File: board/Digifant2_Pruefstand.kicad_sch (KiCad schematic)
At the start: 44 parts, among them J0 VW ECU HARNESS, J1 12V BENCH IN, J2 IDLE VALVE N71, J3 OLED / UI I2C, Q1 2N7002, Q2 P-MOS -30V >=5A, Q3 2N7002, SW1 PUSH, SW2 PUSH, SW3 PUSH, U1 INA226 (0x40), U2 MCP4728 (0x60), U3 INA226 (0x41), U4 AD9833, U5 Raspberry Pi Pico, Y1 25MHz

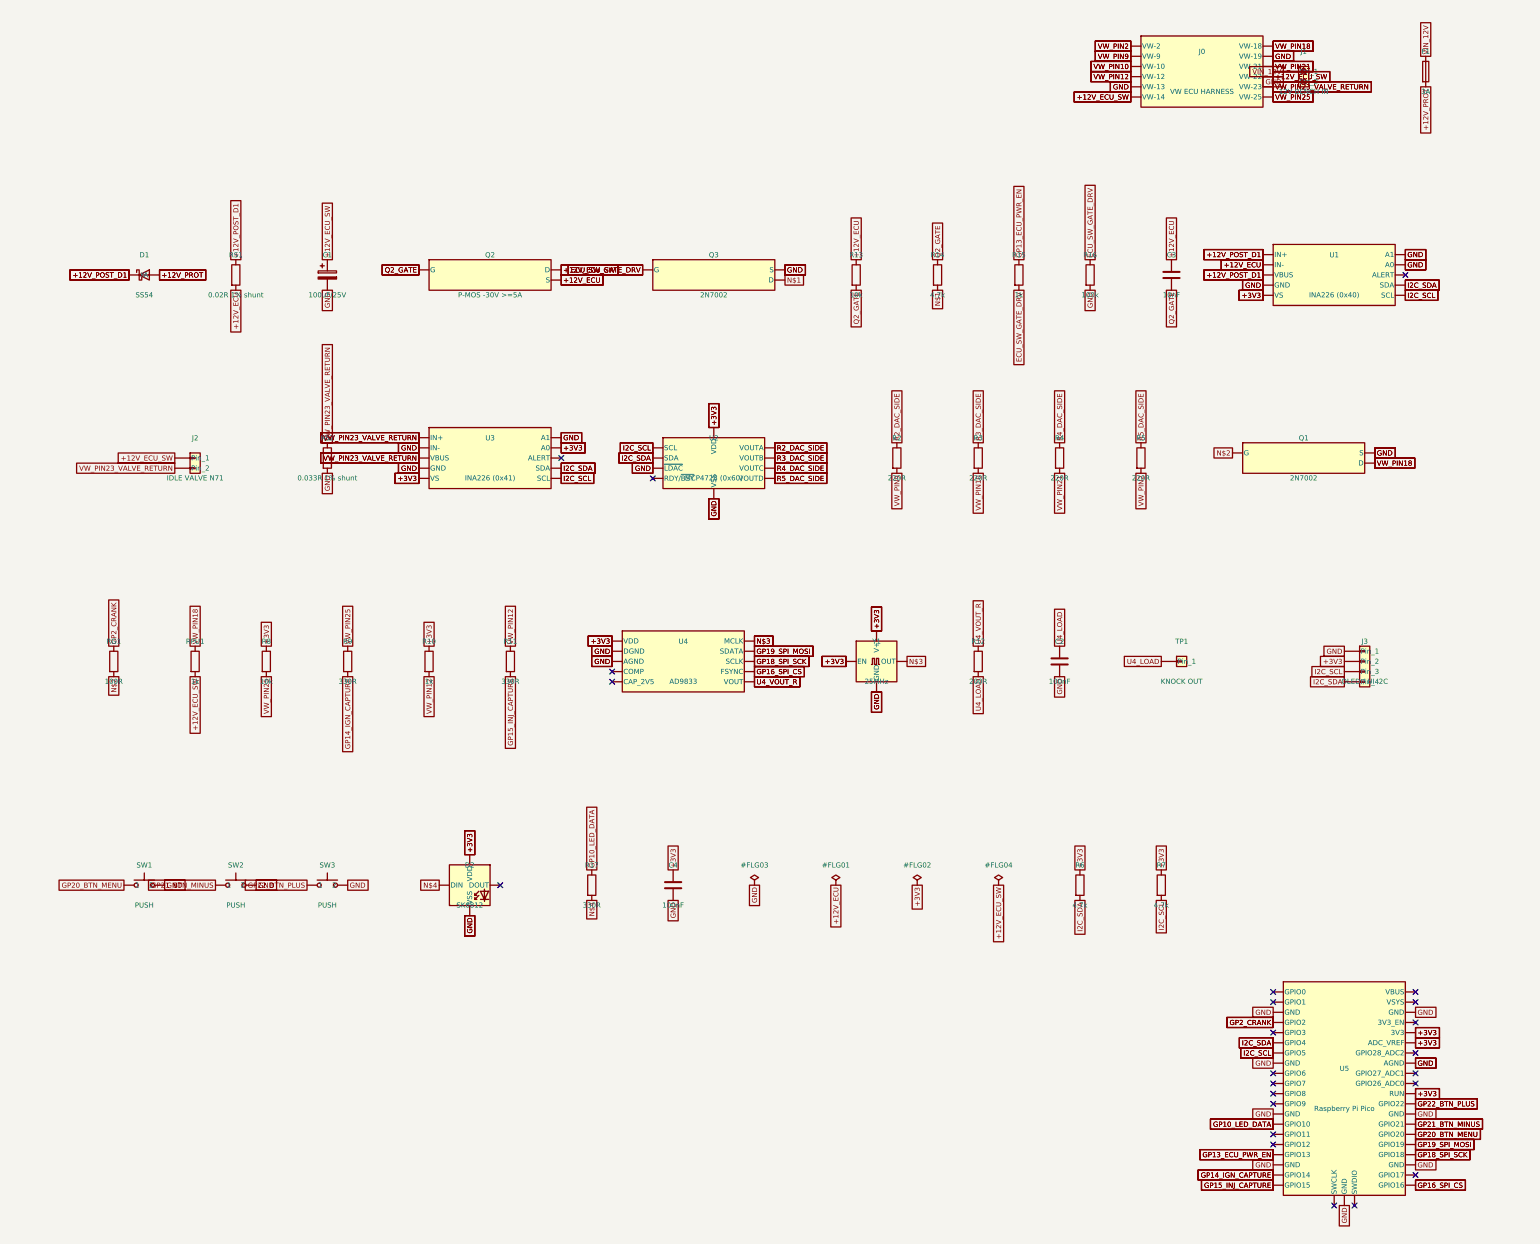
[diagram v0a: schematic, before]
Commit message: Verify VW pinout; add throttle switches, AFM ref sense, bus-voltage read
- verified the harness against the cabby-info.com Digifant II 25-pin reference;
  DESIGN.md now marks each pin confirmed / flagged (VW-8-vs-18 crank, VW-6/11
  idle-vs-WOT unresolved)
- J0 -> 15-pos terminal block; break out VW-6/11 (throttle switches) and VW-17
- throttle_switches(): Q4/Q5 open-drain emulate the idle + WOT micro-switches
  on GP6/GP7, fail-safe open
- afm_ref_sense(): R20/R21 divider + C5 feed VW-17 into GP26/ADC0 so the LMM
  sim can be scaled ratiometrically
- U1 VBUS moved to the shunt load side -> reads the ECU supply voltage;
  U3 VBUS on the valve supply rail -> reads valve feed voltage
- mounting holes flagged board-only (no more extra_footprint DRC)

Co-Authored-By: Claude Sonnet 5 <noreply@anthropic.com>
Claude-Session: https://claude.ai/code/session_01XcEuUwwCT37oProAm8HYeY
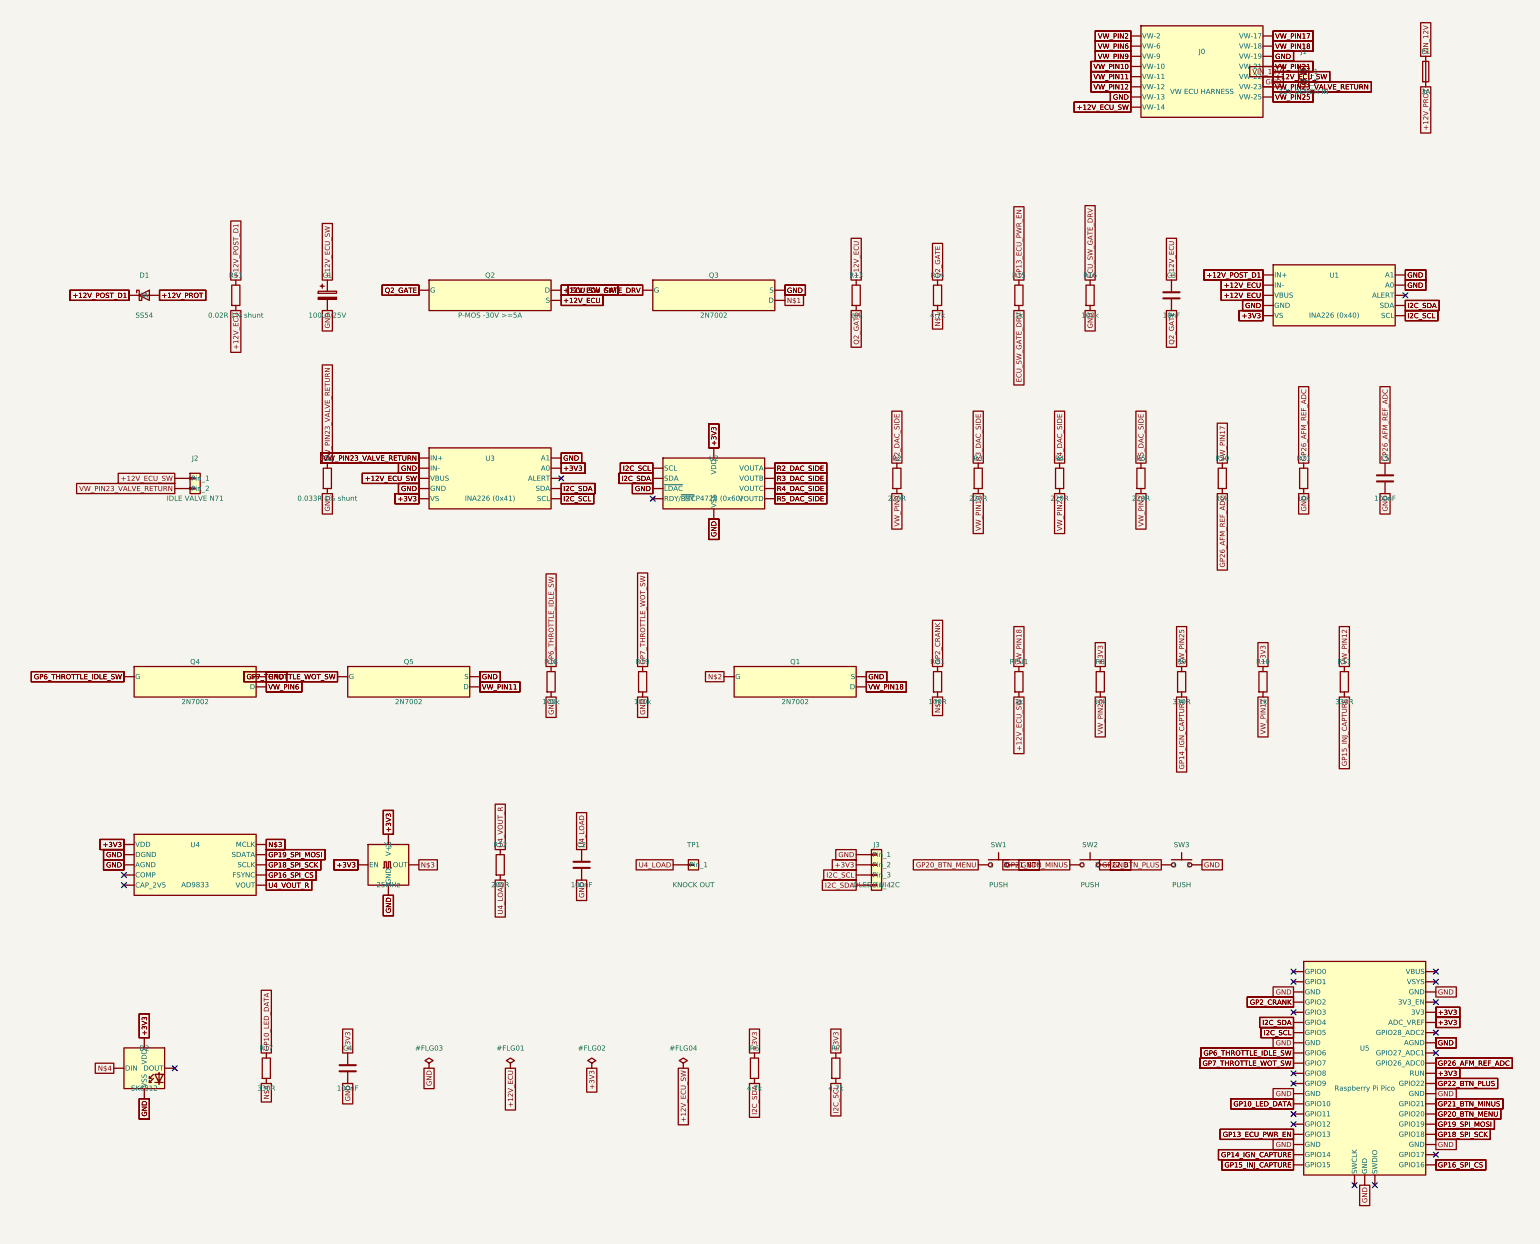
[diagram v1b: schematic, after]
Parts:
- added C5: 100nF, Capacitor_SMD:C_0805_2012Metric, symbol Device:C
- added Q4, Q5: 2N7002, Package_TO_SOT_SMD:SOT-23, symbol Custom_Digifant2:Q_NMOS_2N7002
- added R18, R19: 100k, Resistor_SMD:R_0805_2012Metric, symbol Device:R
- added R20: 15k, Resistor_SMD:R_0805_2012Metric, symbol Device:R
- added R21: 10k, Resistor_SMD:R_0805_2012Metric, symbol Device:R
- J0: footprint TerminalBlock:TerminalBlock_MaiXu_MX126-5.0-12P_1x12_P5.00mm -> TerminalBlock:TerminalBlock_MaiXu_MX126-5.0-15P_1x15_P5.00mm
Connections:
- net +12V_ECU: now also U1.8 (VBUS)
- net +12V_ECU_SW: now also J0.13 (VW-22), J0.8 (VW-14), U3.8 (VBUS); no longer J0.10 (VW-22), J0.6 (VW-14)
- net +12V_POST_D1: no longer U1.8 (VBUS)
- net GND: now also J0.11 (VW-19), J0.7 (VW-13), C5.2, Q4.2 (S), Q5.2 (S), R18.2, R19.2, R21.2; no longer J0.5 (VW-13), J0.8 (VW-19)
- net VW_PIN10: now also J0.4 (VW-10); no longer J0.3 (VW-10)
- net VW_PIN12: now also J0.6 (VW-12); no longer J0.4 (VW-12)
- net VW_PIN18: now also J0.10 (VW-18); no longer J0.7 (VW-18)
- net VW_PIN21: now also J0.12 (VW-21); no longer J0.9 (VW-21)
- net VW_PIN23_VALVE_RETURN: now also J0.14 (VW-23); no longer J0.11 (VW-23), U3.8 (VBUS)
- net VW_PIN25: now also J0.15 (VW-25); no longer J0.12 (VW-25)
- net VW_PIN9: now also J0.3 (VW-9); no longer J0.2 (VW-9)
- net GP7_THROTTLE_WOT_SW: now reaches U5.10 (GPIO7)
- net GP7_THROTTLE_WOT_SW: now also Q5.1 (G), R19.1
- net GP26_AFM_REF_ADC: now reaches U5.31 (GPIO26_ADC0)
- net GP26_AFM_REF_ADC: now also C5.1, R20.2, R21.1
- net GP6_THROTTLE_IDLE_SW: now reaches U5.9 (GPIO6)
- net GP6_THROTTLE_IDLE_SW: now also Q4.1 (G), R18.1
- new net VW_PIN11: J0.5 (VW-11), Q5.3 (D)
- new net VW_PIN17: J0.9 (VW-17), R20.1
- new net VW_PIN6: J0.2 (VW-6), Q4.3 (D)
- no-connect marks 24 -> 21

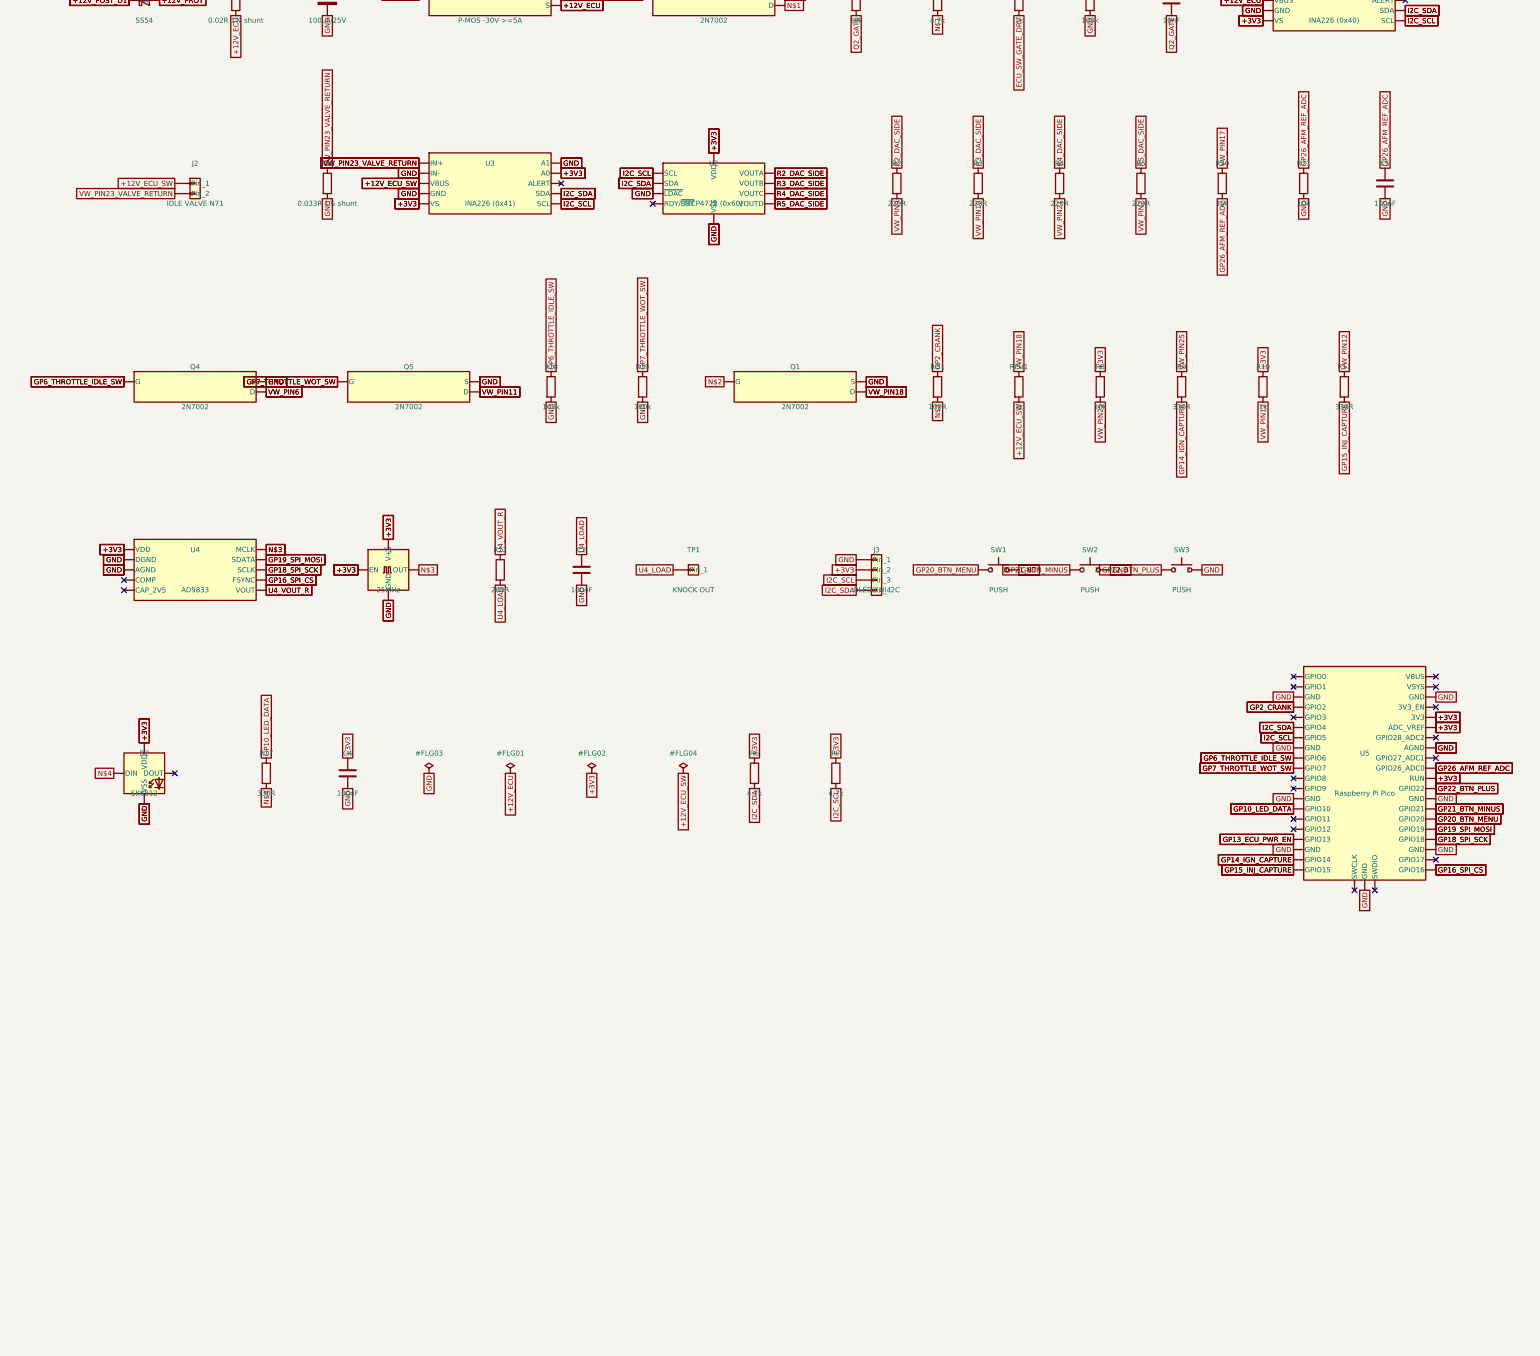
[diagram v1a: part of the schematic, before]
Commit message: Add GPIO open-circuit switches for the lambda and both temp sensors
U6-U8 (TS5A3159A SPDT, ~1 ohm) in series with the intake-air NTC, coolant
NTC and lambda DAC outputs. GPIO high = sensor connected, low = COM floats to
the open NC pin so the ECU sees an open sensor and should fault. R22-R24 pull
the controls up (connected at power-on). Lambda series R 220R -> 1k so it looks
less like an ideal source. GP8/GP9/GP11.

Also: min_hole_clearance 0.25 -> 0.15 (freerouting put a via near the Pico NPTH).

Co-Authored-By: Claude Sonnet 5 <noreply@anthropic.com>
Claude-Session: https://claude.ai/code/session_01XcEuUwwCT37oProAm8HYeY
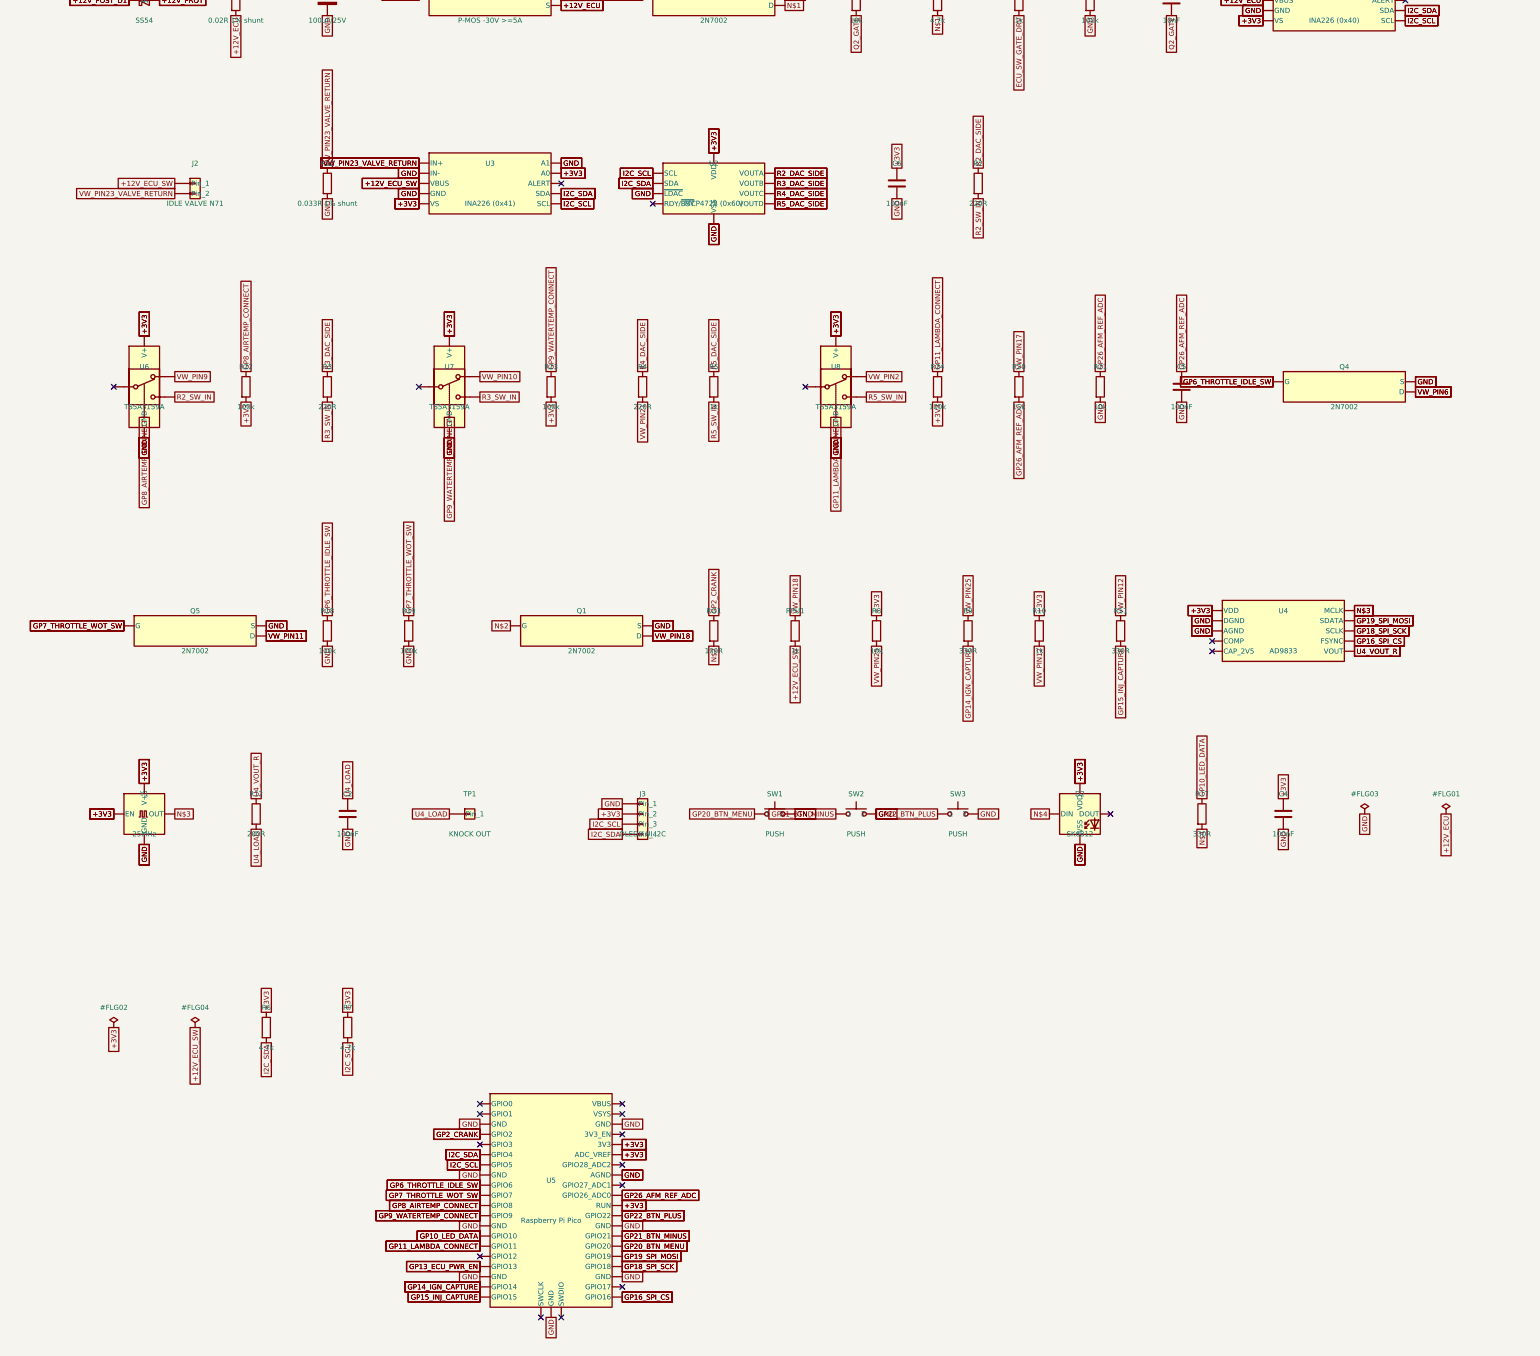
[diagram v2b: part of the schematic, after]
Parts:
- added C6: 100nF, Capacitor_SMD:C_0805_2012Metric, symbol Device:C
- added R22, R23, R24: 100k, Resistor_SMD:R_0805_2012Metric, symbol Device:R
- added U6, U7, U8: TS5A3159A, Package_TO_SOT_SMD:SOT-23-6, symbol Analog_Switch:TS5A3159ADBVR
- R5: value 220R -> 1k
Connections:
- net +3V3: now also C6.1, R22.2, R23.2, R24.2, U6.5 (V+), U7.5 (V+), U8.5 (V+)
- net GND: now also C6.2, U6.2 (GND), U7.2 (GND), U8.2 (GND)
- net VW_PIN10: now also U7.3; no longer R3.2
- net VW_PIN2: now also U8.3; no longer R5.2
- net VW_PIN9: now also U6.3; no longer R2.2
- net GP8_AIRTEMP_CONNECT: now reaches U5.11 (GPIO8)
- net GP8_AIRTEMP_CONNECT: now also R22.1, U6.6
- net GP9_WATERTEMP_CONNECT: now reaches U5.12 (GPIO9)
- net GP9_WATERTEMP_CONNECT: now also R23.1, U7.6
- net GP11_LAMBDA_CONNECT: now reaches U5.15 (GPIO11)
- net GP11_LAMBDA_CONNECT: now also R24.1, U8.6
- new net R2_SW_IN: R2.2, U6.1
- new net R3_SW_IN: R3.2, U7.1
- new net R5_SW_IN: R5.2, U8.1

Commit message: Fix throttle-switch model + give the OLED header real clearance
Corrections sourced from the user's own hands-on Digifant HiL notes:
- VW-6 is sensor/idle-switch common ground, not a 2nd switch contact -- wired
  to GND directly. Only one idle switch, on VW-11 (Q5). Removed Q4/R18/GP7.
- VW-18 confirmed for the crank/Hall signal (needs >=8-10V amplitude per the
  user's own bench notes), resolving the earlier VW-8-vs-18 ambiguity.
- R10 1k injector pull-up validated (their bench found 10k too weak, even
  2.2k marginal).
- Noted VW-3 fuel-pump-relay monitoring and per-signal indicator LEDs as
  possible future additions, per the user's original HiL design.

Also: J3 (OLED header) now gets its own ~40mm clear band at the bottom of the
board, isolated from D2/J2 which used to sit only ~7mm away -- a 0.96" OLED
module plugged in flat would have overhung them. Board grew to 144x154mm.

Co-Authored-By: Claude Sonnet 5 <noreply@anthropic.com>
Claude-Session: https://claude.ai/code/session_01XcEuUwwCT37oProAm8HYeY
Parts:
- removed Q4: 2N7002, Package_TO_SOT_SMD:SOT-23, symbol Custom_Digifant2:Q_NMOS_2N7002
- removed R18: 100k, Resistor_SMD:R_0805_2012Metric, symbol Device:R
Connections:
- net VW_PIN6 is gone; now on net GND: J0.2 (VW-6)
- net GP6_THROTTLE_IDLE_SW: now also Q5.1 (G), R19.1
- removed net GP7_THROTTLE_WOT_SW: Q5.1 (G), R19.1, U5.10 (GPIO7)
- no-connect marks 21 -> 22
